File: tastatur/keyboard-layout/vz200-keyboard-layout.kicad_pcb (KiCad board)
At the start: 2 copper layers, 174.5 x 71.6 mm, 48 parts, among them P1 PWR-LED, SW1 key7, SW10 key-dot, SW11 key9, SW12 key6, SW13 key3, SW14 keyA, SW15 keyF, SW16 keyK, SW17 keyP, SW18 keyU, SW19 keyZ/Y, SW2 key4, SW20 keyB, SW21 keyG, SW22 keyL, SW23 keyQ, SW24 keyV, SW25 key-space, SW26 key-semicolon/Ö, SW27 keyC, SW28 keyH, SW29 keyM, SW3 key1, SW30 keyR, SW31 keyW, SW32 key-apostroph/Ä, SW33 keyD, SW34 keyI, SW35 keyN, SW36 keyS, SW37 keyX, SW38 key-ctrl-left, SW39 key-left-shift, SW4 key-/ß, SW40 keyE, SW41 keyJ, SW42 keyO, SW43 keyT, SW44 keyY/Z, SW45 key-enter, SW5 key-comma, SW6 key8, SW7 key5, SW8 key2, SW9 key0, U1 KeyWarrier24-8Mod

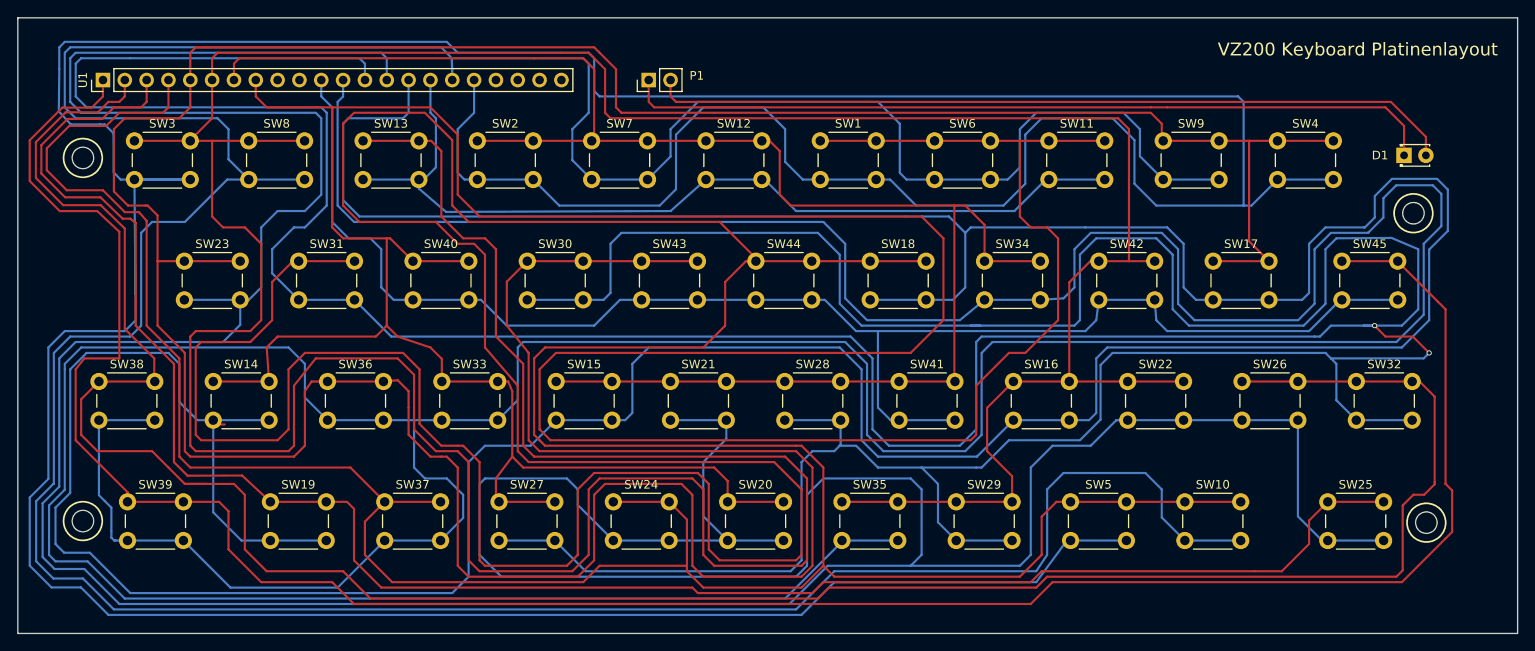
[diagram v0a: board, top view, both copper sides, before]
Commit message: tastatur /emulator: Reset-Taste (ESC) implementiert; Platinenlayout ergänzt und beschriftet
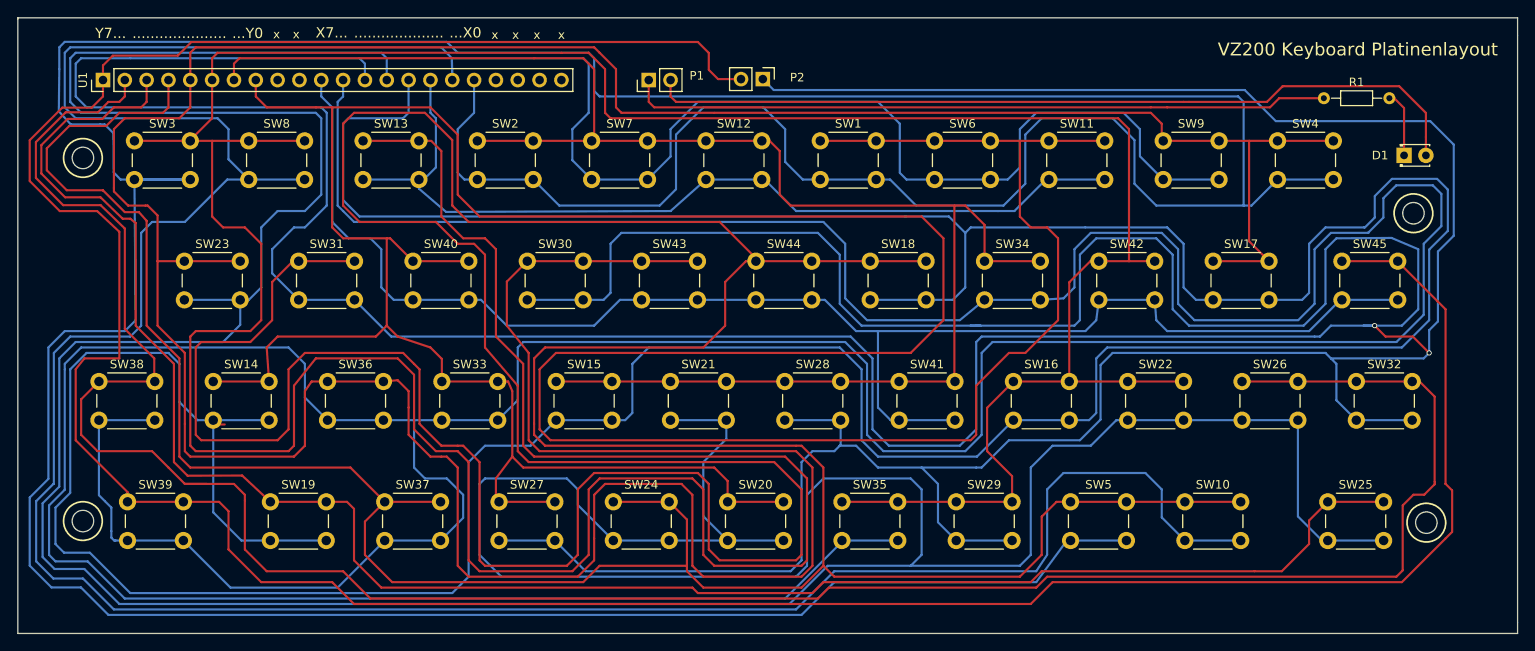
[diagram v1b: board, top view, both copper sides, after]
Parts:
- added P2: Reset-Button, Pin_Headers:Pin_Header_Straight_1x02_Pitch2.54mm, F.Cu at (169.8, 68.6)
- added R1: 110, Resistors_ThroughHole:R_Axial_DIN0204_L3.6mm_D1.6mm_P7.62mm_Horizontal, F.Cu at (235.1, 70.9)
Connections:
- P1 pad 1: Net-(D1-Pad1) -> Net-(P1-Pad1)
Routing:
- net Net-(P2-Pad1): track 585.7 -> 694.7 mm
- net Net-(D1-Pad1): track 95.0 -> 7.69 mm
- net Net-(P1-Pad1): track 0.00 -> 81.8 mm
- net Net-(P2-Pad2): track 274.2 -> 354.2 mm
- net Net-(D1-Pad2): track 93.9 -> 97.0 mm
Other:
- board text added: "...................."
- board text added: "....................."
- board text added: "...X0"
- board text added: "...Y0"
- board text added: "X7..."
- board text added: "Y7..."
- board text added: "x"

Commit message: Repo bereinigen
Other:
- board text added: "Key-Reset"
- board text added: "PWR-LED"
- board text added: "VZ200 Keyboard Platinenlayout - 2019 - Christian Wahlmann"
- board text removed: "VZ200 Keyboard Platinenlayout"
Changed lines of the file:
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@@
     (links 187)
     (no_connects 2)
-    (area 83.042999 61.438999 257.691001 133.217001)
+    (area 17.127 44.567 271.535715 191.073)
     (thickness 1.6)
-    (drawings 37)
+    (drawings 39)
     (tracks 1048)
     (zones 0)
@@
       (effects (font (size 1 1) (thickness 0.15)))
     )
-    (fp_text value PWR-LED (at 2.794 1.524 180) (layer F.Fab)
+    (fp_text value PWR-LED (at -3.002 0.194 180) (layer F.Fab)
       (effects (font (size 1 1) (thickness 0.15)))
     )
@@
       (effects (font (size 1 1) (thickness 0.15)))
     )
-    (fp_text value Reset-Button (at -2.794 0.254 360) (layer F.Fab)
+    (fp_text value Reset-Button (at 2.667 0.254 360) (layer F.Fab)
       (effects (font (size 1 1) (thickness 0.15)))
     )
@@
     )
   )
+  (gr_text Key-Reset (at 168.783 65.5955) (layer F.SilkS)
+    (effects (font (size 1.2 1.2) (thickness 0.3)))
+  )
+  (gr_text PWR-LED (at 158.0515 65.7225) (layer F.SilkS)
+    (effects (font (size 1.2 1.2) (thickness 0.25)))
+  )
   (gr_text .................... (at 127.4445 63.246) (layer F.SilkS)
     (effects (font (size 1.2 1.2) (thickness 0.3)))
@@
   )
   (gr_line (start 83.118 61.514) (end 83.118 61.641) (angle 90) (layer Edge.Cuts) (width 0.15))
-  (gr_text "VZ200 Keyboard Platinenlayout" (at 255.33 65.197) (layer F.SilkS)
+  (gr_text "VZ200 Keyboard Platinenlayout - 2019 - Christian Wahlmann" (at 254.9525 65.151) (layer F.SilkS)
     (effects (font (size 1.5 1.5) (thickness 0.3)) (justify right))
   )

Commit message: Screenshots Monitor Anleitung
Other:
- rule via_min_drill: 0.3 -> 0.4
- rule via_min_size: 0.4 -> 0.6
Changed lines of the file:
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@@
     (via_size 0.6)
     (via_drill 0.4)
-    (via_min_size 0.4)
-    (via_min_drill 0.3)
+    (via_min_size 0.6)
+    (via_min_drill 0.4)
     (uvia_size 0.3)
     (uvia_drill 0.1)
     (uvias_allowed no)
-    (uvia_min_size 0.2)
+    (uvia_min_size 0.3)
     (uvia_min_drill 0.1)
     (pcb_text_width 0.3)
